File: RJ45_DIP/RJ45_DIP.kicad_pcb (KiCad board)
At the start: 2 copper layers, 38.1 x 16.5 mm, 3 parts, among them J1 I2C, J2 SOLAR_MOTOR, U1 7810-8P8C

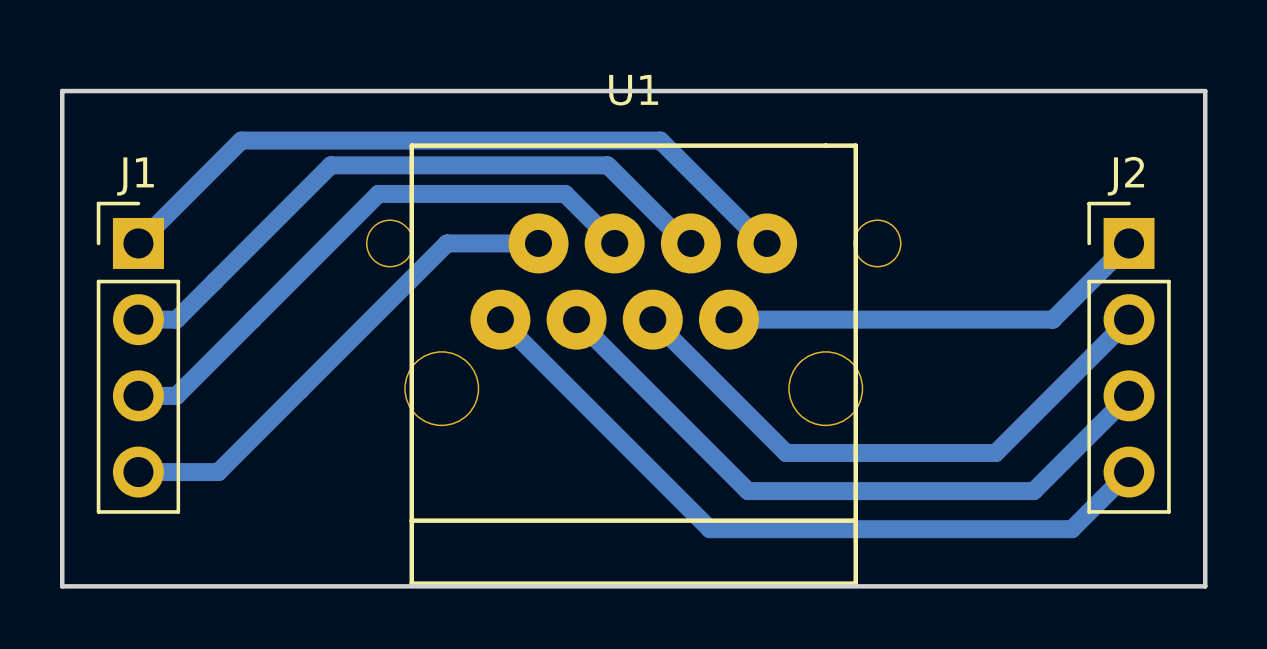
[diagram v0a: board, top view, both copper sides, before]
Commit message: 基板を印刷して入ることを確認した（ちょっと固い）
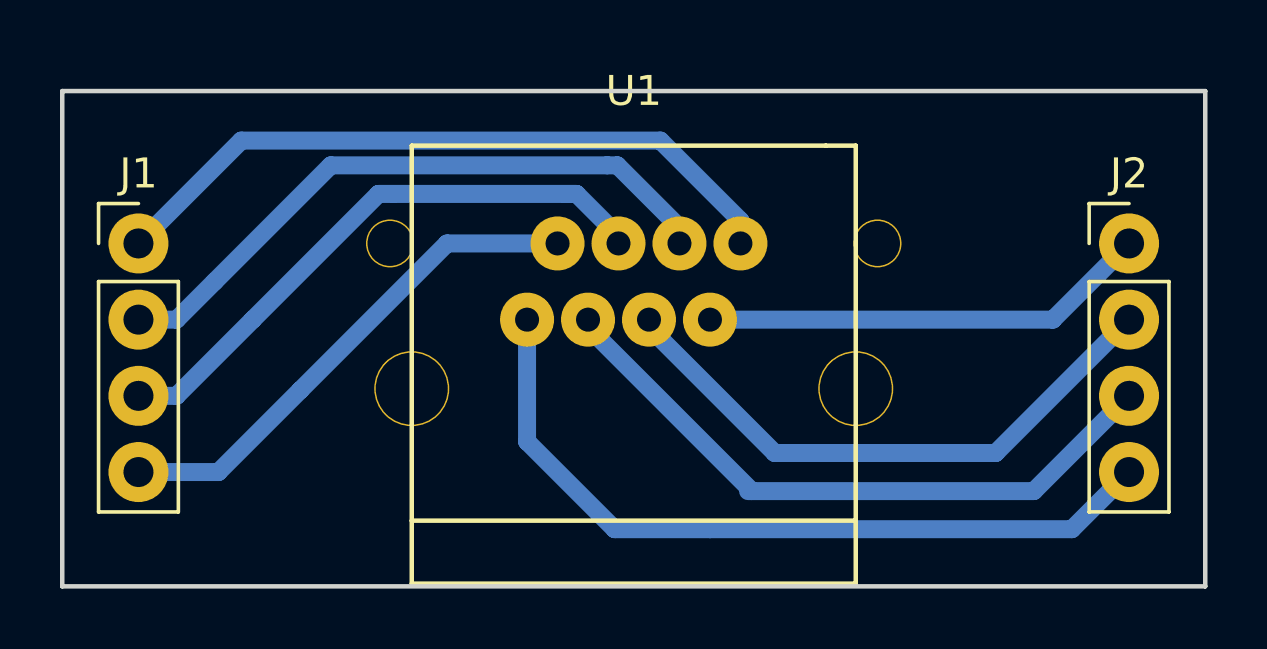
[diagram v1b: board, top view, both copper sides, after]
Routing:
- net Net-(J2-Pad4): track 24.6 -> 26.1 mm
- net Net-(J1-Pad4): track 16.6 -> 17.2 mm
- net Net-(J2-Pad1): track 14.4 -> 15.0 mm
